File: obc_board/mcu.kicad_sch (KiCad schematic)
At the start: 47 parts, among them J4 Micro_SD_Card, U24 TLE9250X, U25 STM32L552ZET6Q, U26 IS66WVH16M8DBLL-100B1LI, Y2 16MHz, Y3 32.768kHz

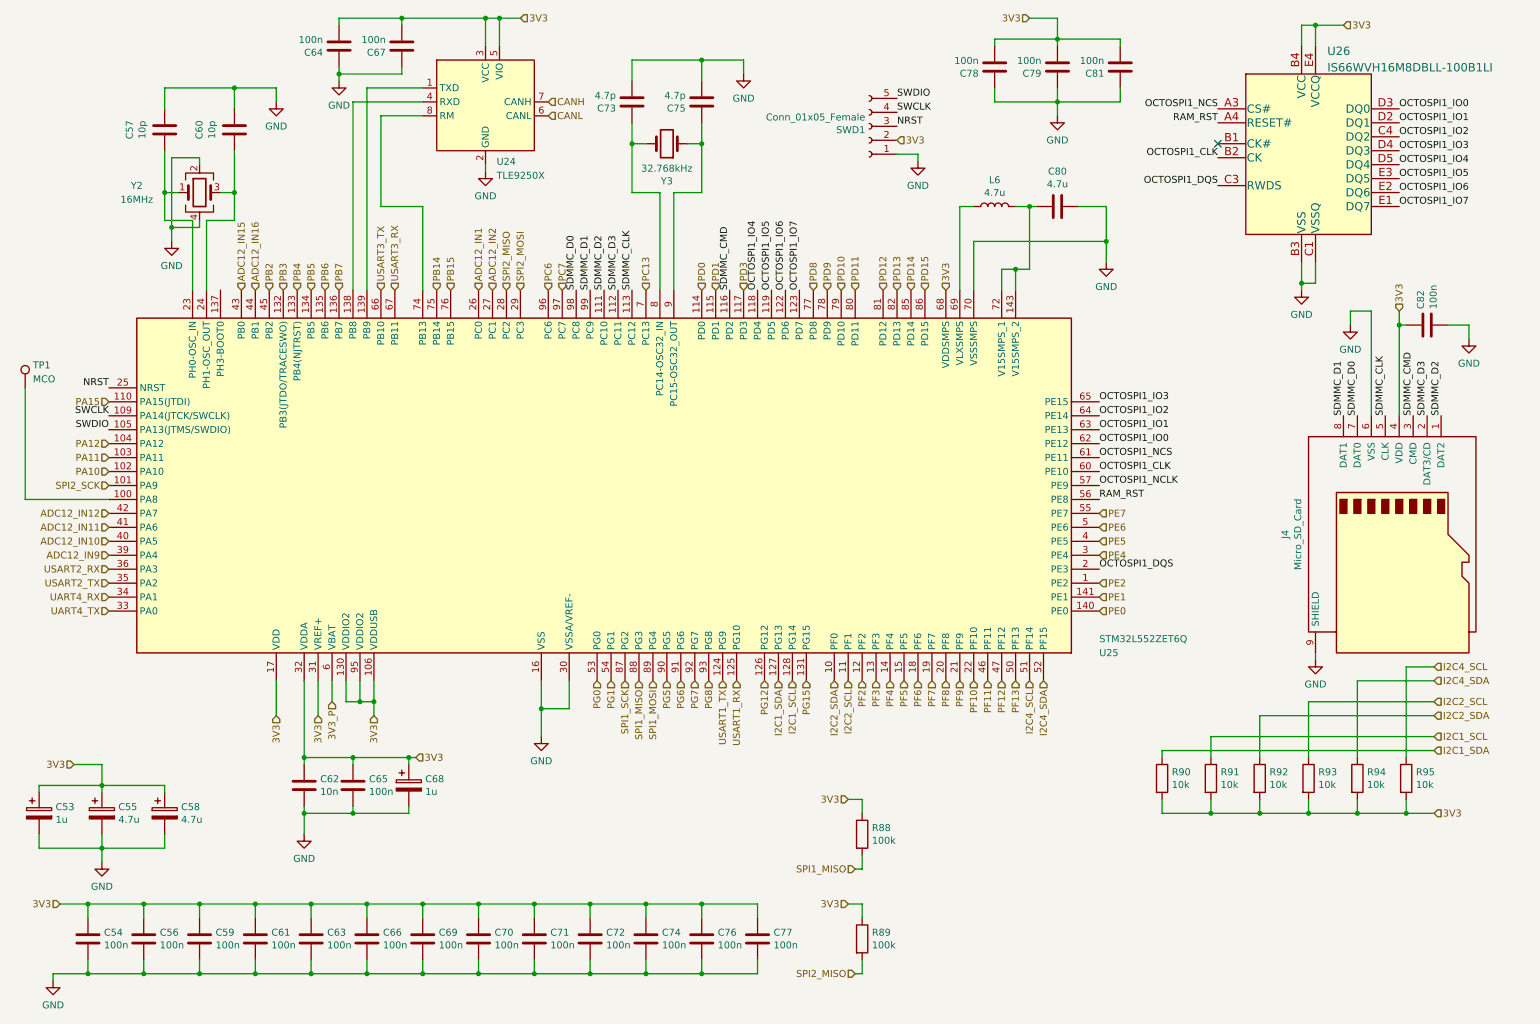
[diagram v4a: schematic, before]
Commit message: routed most of board
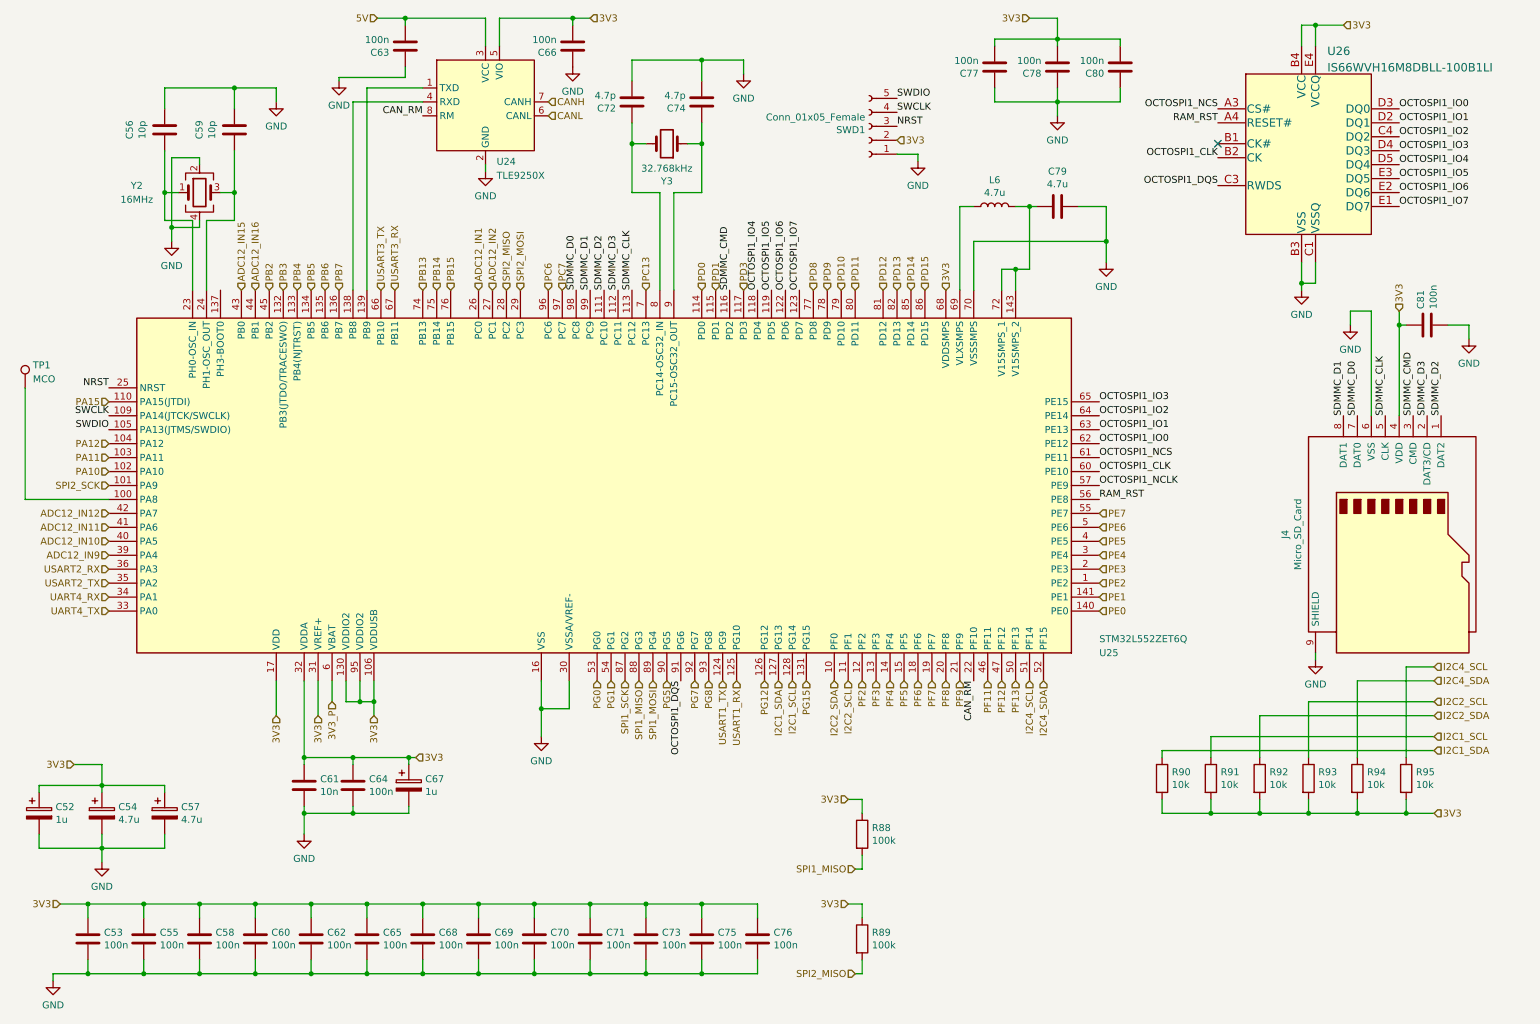
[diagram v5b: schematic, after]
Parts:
- renumbered C53 to C52, C54 to C53, C55 to C54, C56 to C55, C57 to C56, C58 to C57, C59 to C58, C60 to C59, C61 to C60, C62 to C61, C63 to C62, C64 to C63, C65 to C64, C66 to C65, C67 to C66, C68 to C67, C69 to C68, C70 to C69, C71 to C70, C72 to C71, C73 to C72, C74 to C73, C75 to C74, C76 to C75, C77 to C76, C78 to C77, C79 to C78, C80 to C79, C81 to C80, C82 to C81
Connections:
- net PF10 is gone; now on net CAN_RM: U25.22 (PF10)
- net PG6 is gone; now on net OCTOSPI1_DQS: U25.91 (PG6)
- net GND: now also U24.9 (GND)
- net OCTOSPI1_DQS: no longer U25.2 (PE3)
- net VCCQ: no longer C63.2, U24.3 (VCC)
- net CAN_RM: now reaches U24.8 (RM)
- net CAN_RM: no longer U25.74 (PB13)
- new net 5V: C63.2, U24.3 (VCC)
- new net PB13: U25.74 (PB13)
- new net PE3: U25.2 (PE3)
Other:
- moved on the sheet: C63, C66

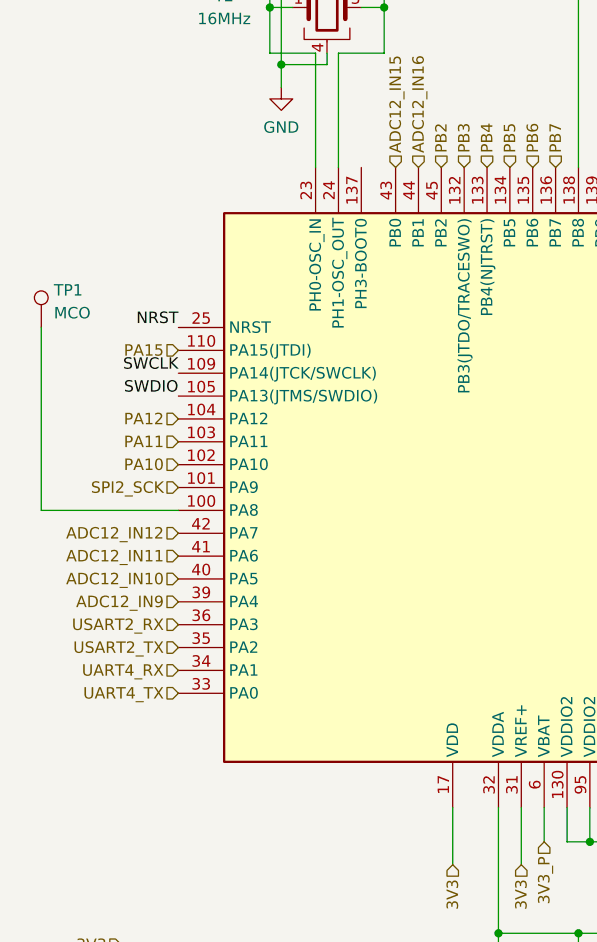
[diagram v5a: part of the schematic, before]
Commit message: added silkscreen labels and gerber file
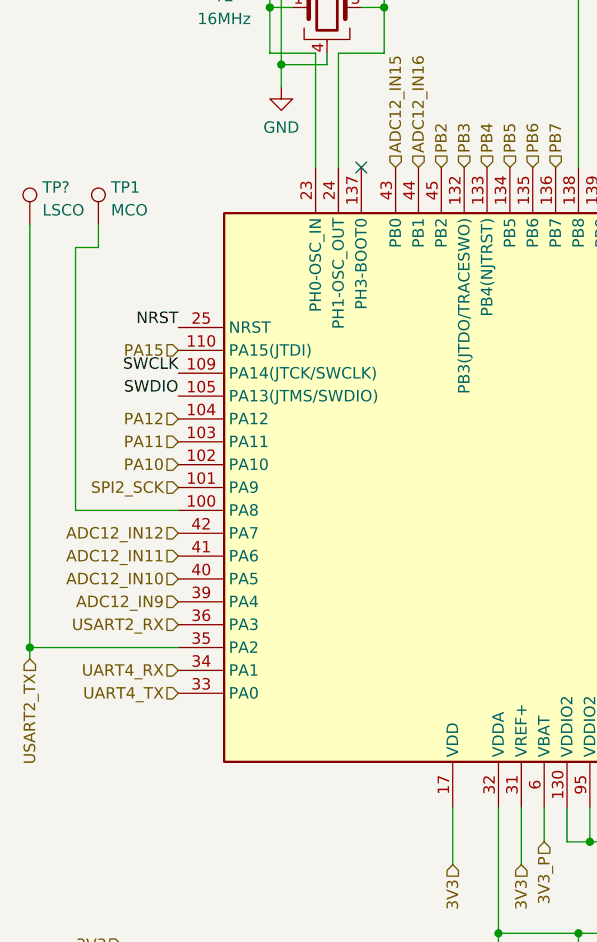
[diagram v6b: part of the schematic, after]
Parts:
- added TP?: LSCO, TestPoint:TestPoint_Pad_D1.5mm, symbol Connector:TestPoint
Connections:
- net USART2_TX: now also TP?.1
- no-connect marks 1 -> 2
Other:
- moved on the sheet: TP1
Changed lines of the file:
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@@
   (junction (at 203.2 19.05) (diameter 0) (color 0 0 0 0)
   )
+  (junction (at 13.97 118.11) (diameter 0) (color 0 0 0 0)
+  )
+  (no_connect (at 50.8 64.77))
   (no_connect (at 232.41 38.1))
   (wire (pts (xy 109.22 135.89) (xy 109.22 140.97))
@@
     (stroke (width 0) (type default) (color 0 0 0 0))
   )
+  (wire (pts (xy 21.59 73.66) (xy 21.59 71.12))
+    (stroke (width 0) (type default) (color 0 0 0 0))
+  )
   (wire (pts (xy 250.19 16.51) (xy 250.19 20.32))
     (stroke (width 0) (type default) (color 0 0 0 0))
@@
     (stroke (width 0) (type default) (color 0 0 0 0))
   )
+  (wire (pts (xy 30.48 102.87) (xy 19.05 102.87))
+    (stroke (width 0) (type default) (color 0 0 0 0))
+  )
   (wire (pts (xy 231.14 146.05) (xy 271.78 146.05))
     (stroke (width 0) (type default) (color 0 0 0 0))
@@
     (stroke (width 0) (type default) (color 0 0 0 0))
   )
+  (wire (pts (xy 30.48 118.11) (xy 13.97 118.11))
+    (stroke (width 0) (type default) (color 0 0 0 0))
+  )
   (wire (pts (xy 36.83 186.69) (xy 36.83 189.23))
     (stroke (width 0) (type default) (color 0 0 0 0))
@@
     (stroke (width 0) (type default) (color 0 0 0 0))
   )
+  (wire (pts (xy 13.97 71.12) (xy 13.97 118.11))
+    (stroke (width 0) (type default) (color 0 0 0 0))
+  )
   (wire (pts (xy 40.64 27.94) (xy 40.64 31.75))
     (stroke (width 0) (type default) (color 0 0 0 0))
@@
     (stroke (width 0) (type default) (color 0 0 0 0))
   )
+  (wire (pts (xy 13.97 118.11) (xy 13.97 119.38))
+    (stroke (width 0) (type default) (color 0 0 0 0))
+  )
   (wire (pts (xy 138.43 34.29) (xy 138.43 38.1))
     (stroke (width 0) (type default) (color 0 0 0 0))
@@
     (stroke (width 0) (type default) (color 0 0 0 0))
   )
+  (wire (pts (xy 19.05 73.66) (xy 21.59 73.66))
+    (stroke (width 0) (type default) (color 0 0 0 0))
+  )
   (wire (pts (xy 128.27 176.53) (xy 138.43 176.53))
     (stroke (width 0) (type default) (color 0 0 0 0))
@@
     (stroke (width 0) (type default) (color 0 0 0 0))
   )
+  (wire (pts (xy 19.05 73.66) (xy 19.05 102.87))
+    (stroke (width 0) (type default) (color 0 0 0 0))
+  )
   (wire (pts (xy 128.27 176.53) (xy 128.27 179.07))
     (stroke (width 0) (type default) (color 0 0 0 0))
@@
     (stroke (width 0) (type default) (color 0 0 0 0))
   )
-  (wire (pts (xy 15.24 82.55) (xy 15.24 102.87))
-    (stroke (width 0) (type default) (color 0 0 0 0))
-  )
   (wire (pts (xy 97.79 189.23) (xy 107.95 189.23))
-    (stroke (width 0) (type default) (color 0 0 0 0))
-  )
-  (wire (pts (xy 15.24 102.87) (xy 30.48 102.87))
     (stroke (width 0) (type default) (color 0 0 0 0))
   )
@@
     (effects (font (size 1.27 1.27)) (justify right))
   )
-  (hierarchical_label "USART2_TX" (shape input) (at 30.48 118.11 180)
+  (hierarchical_label "USART2_TX" (shape input) (at 13.97 119.38 270)
     (effects (font (size 1.27 1.27)) (justify right))
   )
@@
     (pin "1")
   )
+  (symbol (lib_id "Connector:TestPoint") (at 13.97 71.12 0) (unit 1)
+    (in_bom yes) (on_board yes) (fields_autoplaced)
+    (property "Reference" "TP?" (id 0) (at 15.367 66.9833 0)
+      (effects (font (size 1.27 1.27)) (justify left))
+    )
+    (property "Value" "LSCO" (id 1) (at 15.367 69.5202 0)
+      (effects (font (size 1.27 1.27)) (justify left))
+    )
+    (property "Footprint" "TestPoint:TestPoint_Pad_D1.5mm" (id 2) (at 19.05 71.12 0)
+      (effects (font (size 1.27 1.27)) hide)
+    )
+    (property "Datasheet" "~" (id 3) (at 19.05 71.12 0)
+      (effects (font (size 1.27 1.27)) hide)
+    )
+    (pin "1")
+  )
   (symbol (lib_id "power:GND") (at 29.21 168.91 0) (unit 1)
     (in_bom yes) (on_board yes) (fields_autoplaced)
@@
     (pin "2")
   )
-  (symbol (lib_id "Connector:TestPoint") (at 15.24 82.55 0) (unit 1)
+  (symbol (lib_id "Connector:TestPoint") (at 21.59 71.12 0) (unit 1)
     (in_bom yes) (on_board yes) (fields_autoplaced)
-    (property "Reference" "TP1" (id 0) (at 16.637 78.4133 0)
-      (effects (font (size 1.27 1.27)) (justify left))
-    )
-    (property "Value" "MCO" (id 1) (at 16.637 80.9502 0)
-      (effects (font (size 1.27 1.27)) (justify left))
-    )
-    (property "Footprint" "TestPoint:TestPoint_Pad_D1.5mm" (id 2) (at 20.32 82.55 0)
-      (effects (font (size 1.27 1.27)) hide)
-    )
-    (property "Datasheet" "~" (id 3) (at 20.32 82.55 0)
-      (effects (font (size 1.27 1.27)) hide)
-    )
+    (property "Reference" "TP1" (id 0) (at 22.987 66.9833 0)
+      (effects (font (size 1.27 1.27)) (justify left))
+    )
+    (property "Value" "MCO" (id 1) (at 22.987 69.5202 0)
+      (effects (font (size 1.27 1.27)) (justify left))
+    )
+    (property "Footprint" "TestPoint:TestPoint_Pad_D1.5mm" (id 2) (at 26.67 71.12 0)
+      (effects (font (size 1.27 1.27)) hide)
+    )
+    (property "Datasheet" "~" (id 3) (at 26.67 71.12 0)
+      (effects (font (size 1.27 1.27)) hide)
+    )

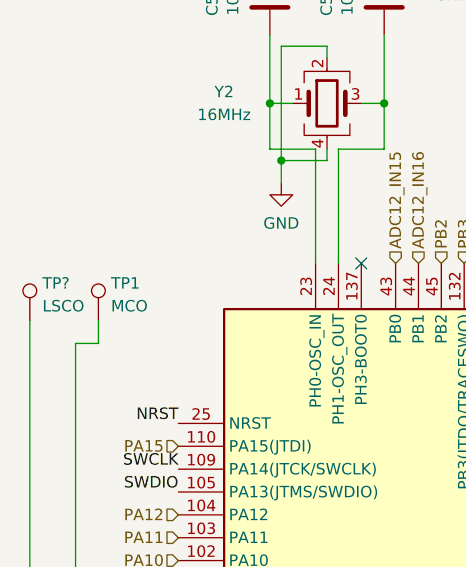
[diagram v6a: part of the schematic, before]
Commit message: added coordinate labels
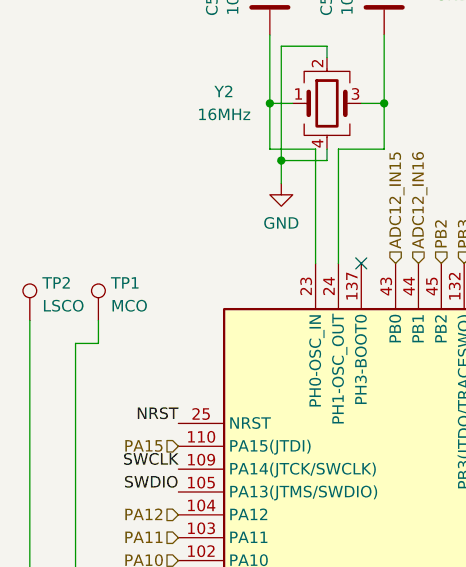
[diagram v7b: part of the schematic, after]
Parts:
- TP1: now left out of the parts list
- TP2: renamed from TP?; now left out of the parts list
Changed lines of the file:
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@@
   )
   (symbol (lib_id "Connector:TestPoint") (at 13.97 71.12 0) (unit 1)
-    (in_bom yes) (on_board yes) (fields_autoplaced)
-    (property "Reference" "TP?" (id 0) (at 15.367 66.9833 0)
+    (in_bom no) (on_board yes) (fields_autoplaced)
+    (property "Reference" "TP2" (id 0) (at 15.367 66.9833 0)
       (effects (font (size 1.27 1.27)) (justify left))
     )
@@
   )
   (symbol (lib_id "Connector:TestPoint") (at 21.59 71.12 0) (unit 1)
-    (in_bom yes) (on_board yes) (fields_autoplaced)
+    (in_bom no) (on_board yes) (fields_autoplaced)
     (property "Reference" "TP1" (id 0) (at 22.987 66.9833 0)
       (effects (font (size 1.27 1.27)) (justify left))

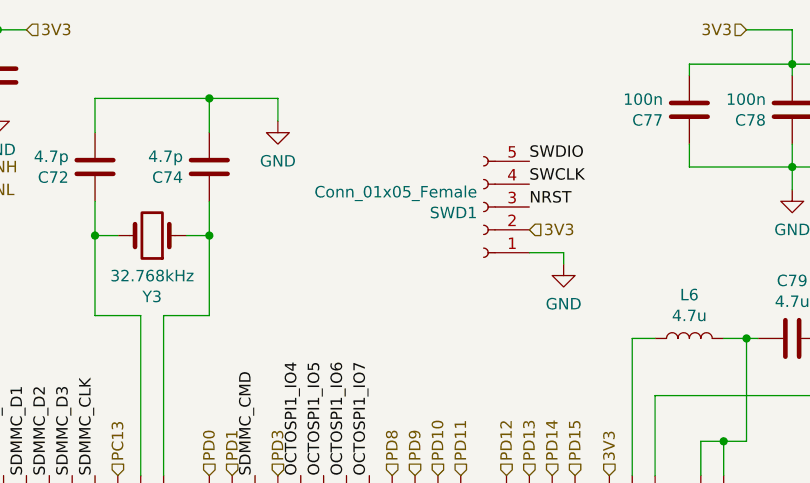
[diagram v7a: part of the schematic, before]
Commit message: changed picoblade symbols to include mounting pins, added photodiode circuitry and additional testpoints, added GPS to FTDI jumper
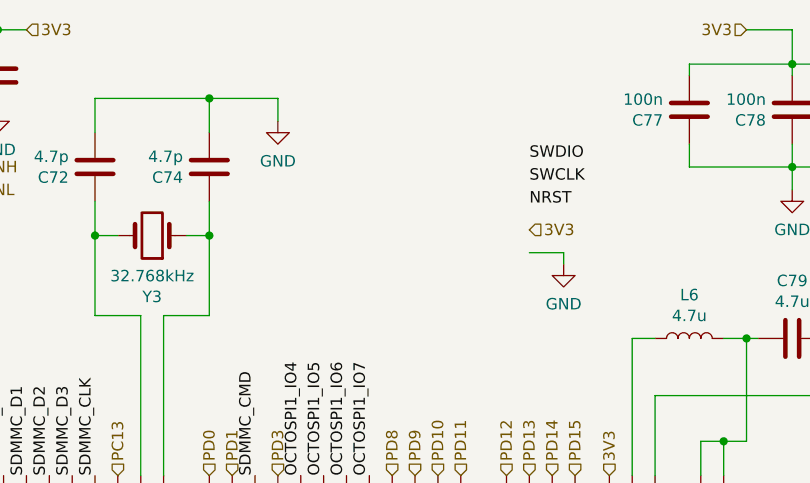
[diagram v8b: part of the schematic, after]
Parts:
- removed SWD1: Conn_01x05_Female, Connector_Molex:Molex_PicoBlade_53261-0571_1x05-1MP_P1.25mm_Horizontal, symbol Connector:Conn_01x05_Female
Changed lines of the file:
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@@
     (pin "2")
-  )
-  (symbol (lib_id "Connector:Conn_01x05_Female") (at 168.91 34.925 180) (unit 1)
-    (in_bom yes) (on_board yes)
-    (property "Reference" "SWD1" (id 0) (at 168.1988 35.5854 0)
-      (effects (font (size 1.27 1.27)) (justify left))
-    )
-    (property "Value" "Conn_01x05_Female" (id 1) (at 168.1988 33.274 0)
-      (effects (font (size 1.27 1.27)) (justify left))
-    )
-    (property "Footprint" "Connector_Molex:Molex_PicoBlade_53261-0571_1x05-1MP_P1.25mm_Horizontal" (id 2) (at 168.91 34.925 0)
-      (effects (font (size 1.27 1.27)) hide)
-    )
-    (property "Datasheet" "~" (id 3) (at 168.91 34.925 0)
-      (effects (font (size 1.27 1.27)) hide)
-    )
-    (property "Digikey Part Number" "WM26499CT-ND" (id 4) (at 168.91 34.925 0)
-      (effects (font (size 1.27 1.27)) hide)
-    )
-    (pin "1")
-    (pin "2")
-    (pin "3")
-    (pin "4")
-    (pin "5")
   )
   (symbol (lib_id "Device:Crystal_GND24") (at 46.99 46.99 0) (unit 1)
